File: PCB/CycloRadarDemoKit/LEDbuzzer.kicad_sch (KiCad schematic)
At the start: 27 parts, among them Q301 L8050QLT1G

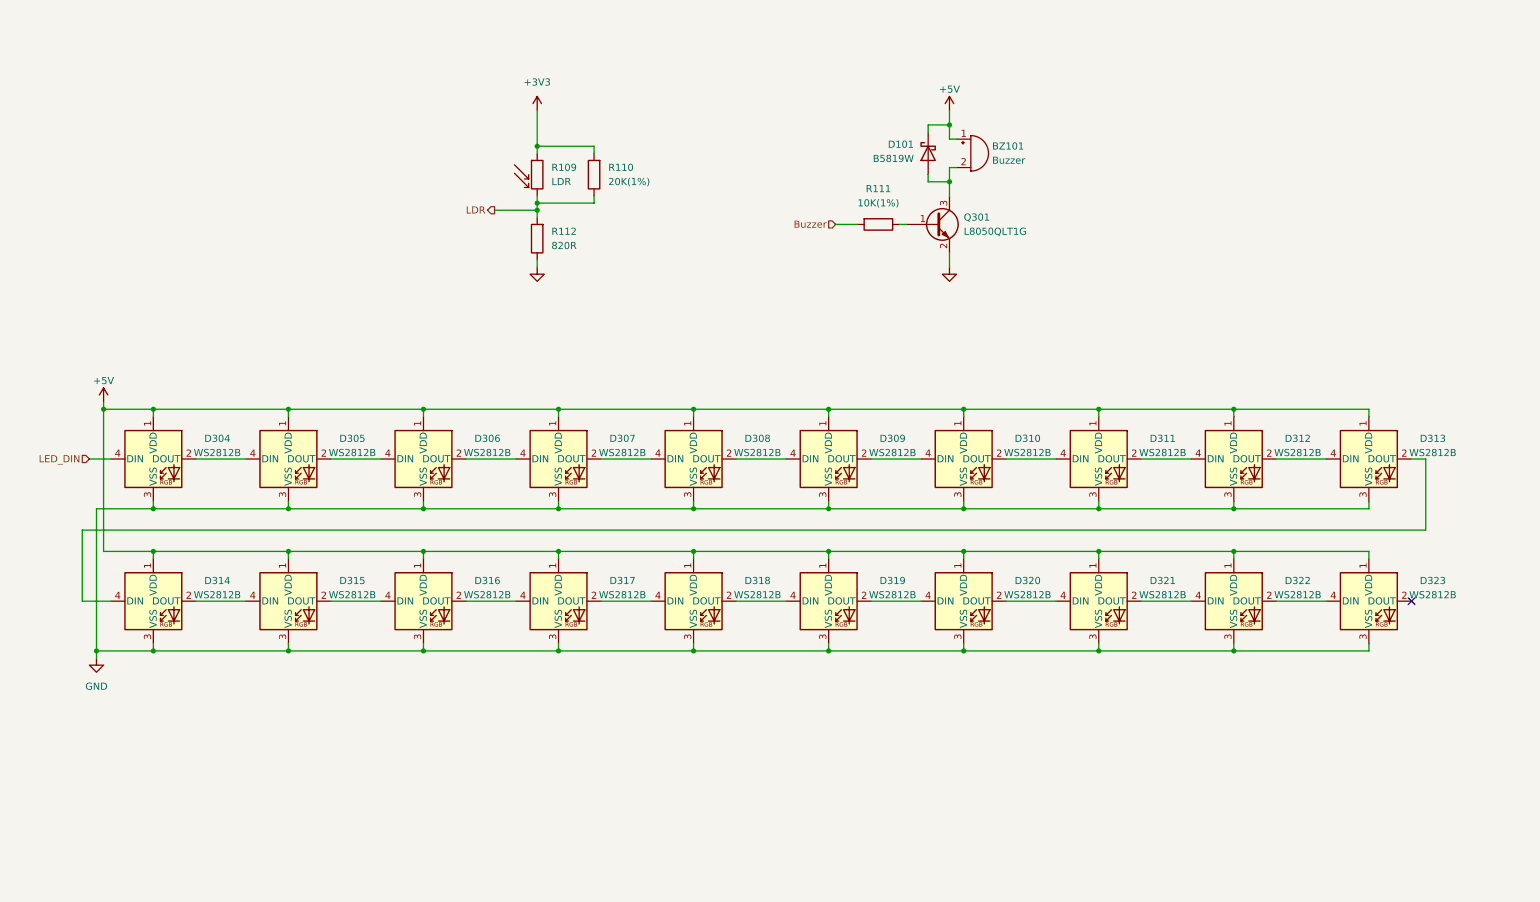
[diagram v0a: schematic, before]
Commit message: Schematic edited, split sheets
improved PM diagram
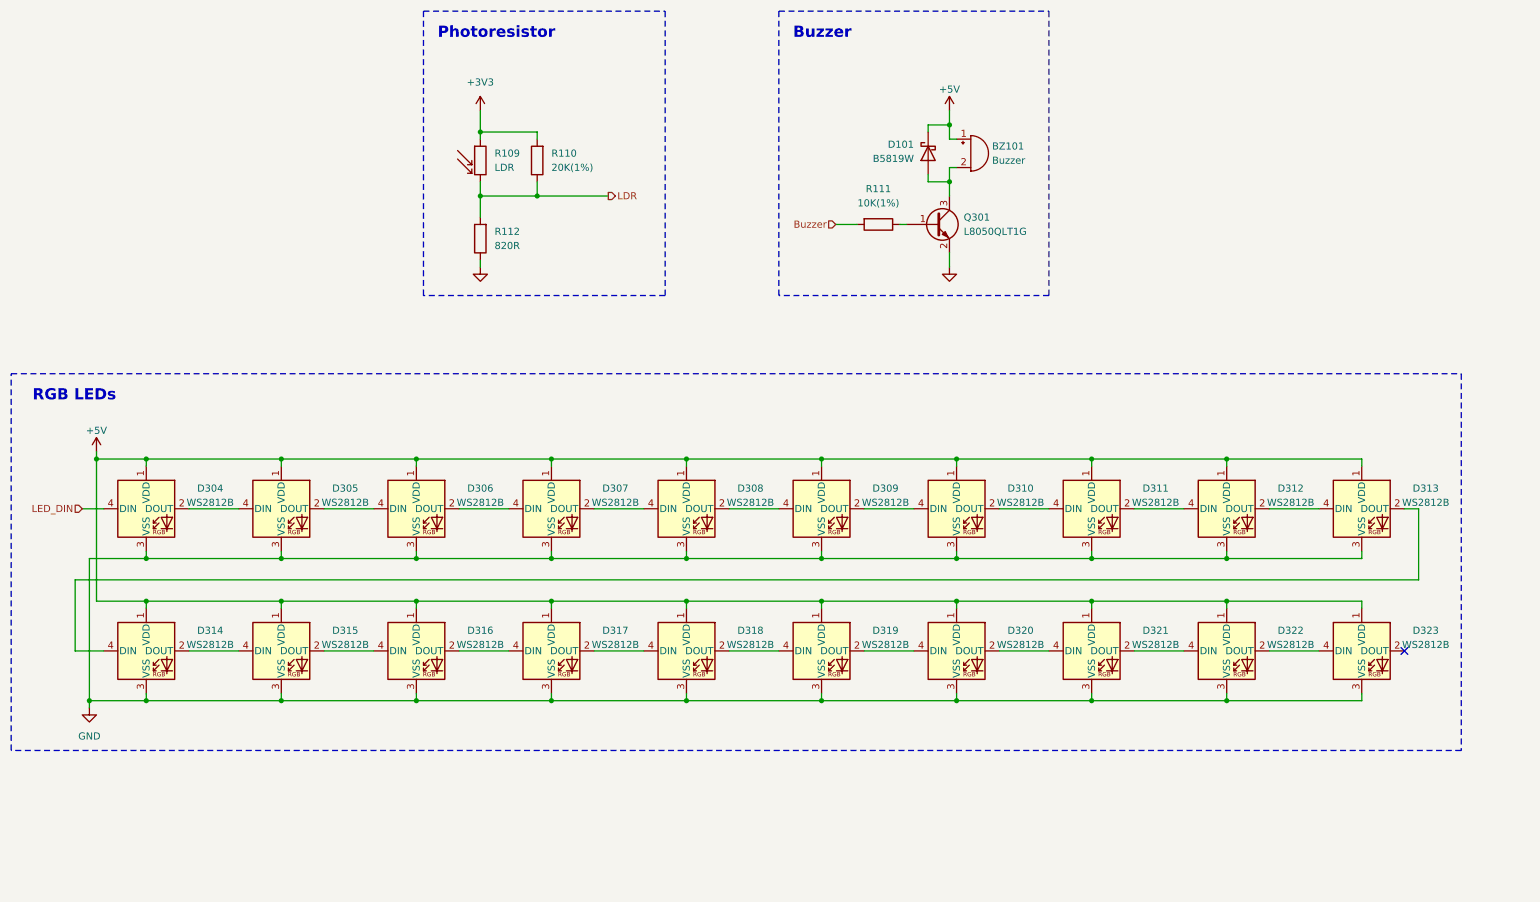
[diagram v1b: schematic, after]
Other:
- note added: "Buzzer"
- note added: "Photoresistor"
- note added: "RGB LEDs"
- moved on the sheet: D304, D305, D306, D307, D308, D309, D310, D311, D312, D313, D314, D315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

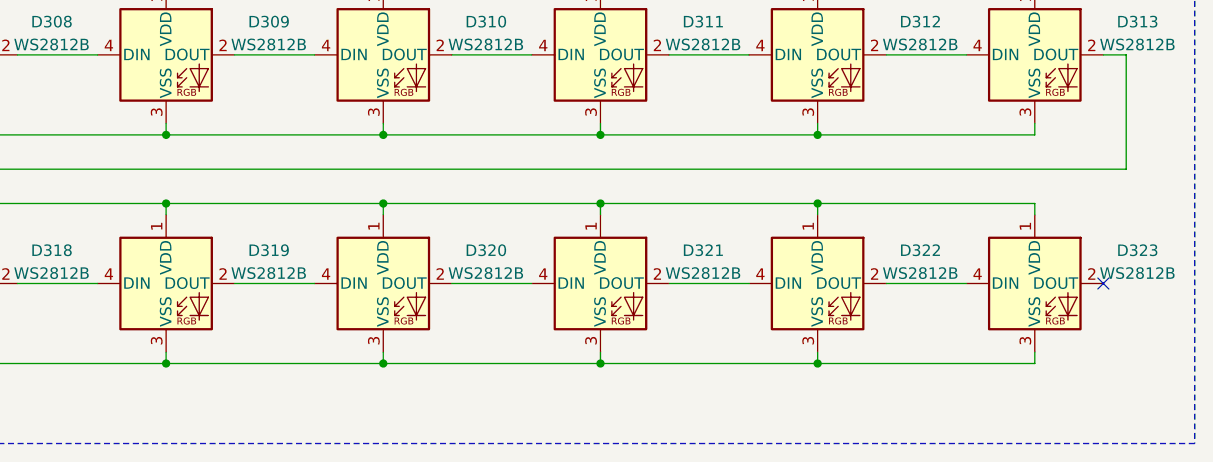
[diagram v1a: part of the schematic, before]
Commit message: layout mockup done
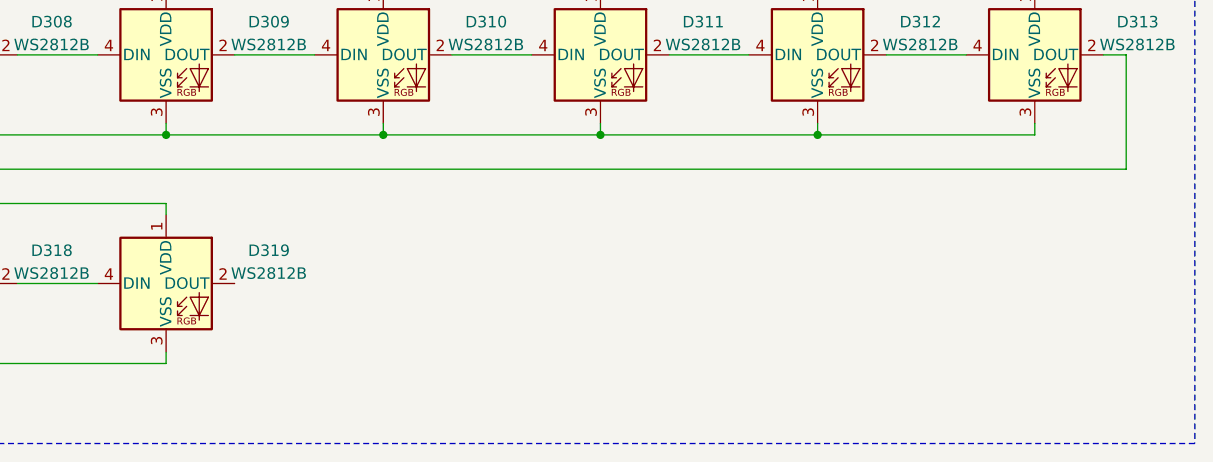
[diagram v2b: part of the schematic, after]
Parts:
- removed D320, D321, D322, D323: WS2812B, LED_SMD:LED_SK6812MINI_PLCC4_3.5x3.5mm_P1.75mm, symbol LED:WS2812B
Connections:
- no-connect marks 1 -> 0

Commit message: PCB, 3Dmodel
mockup PCB version done, schcematic exported to latex, 3D model generated and exported to latex
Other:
- title: Safety Ride Radar Sensor -> Radar Safety Sensor
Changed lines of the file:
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@@
   (paper "A4")
   (title_block
-    (title "Safety Ride Radar Sensor")
-    (date "2023-12-19")
-    (rev "Rev.: WIP")
+    (title "Radar Safety Sensor")
+    (date "2023-12-20")
+    (rev "Rev.: 1")
     (company "ALPS Electric Czech, s.r.o.")
     (comment 1 "Designed by Martin Tavoda")

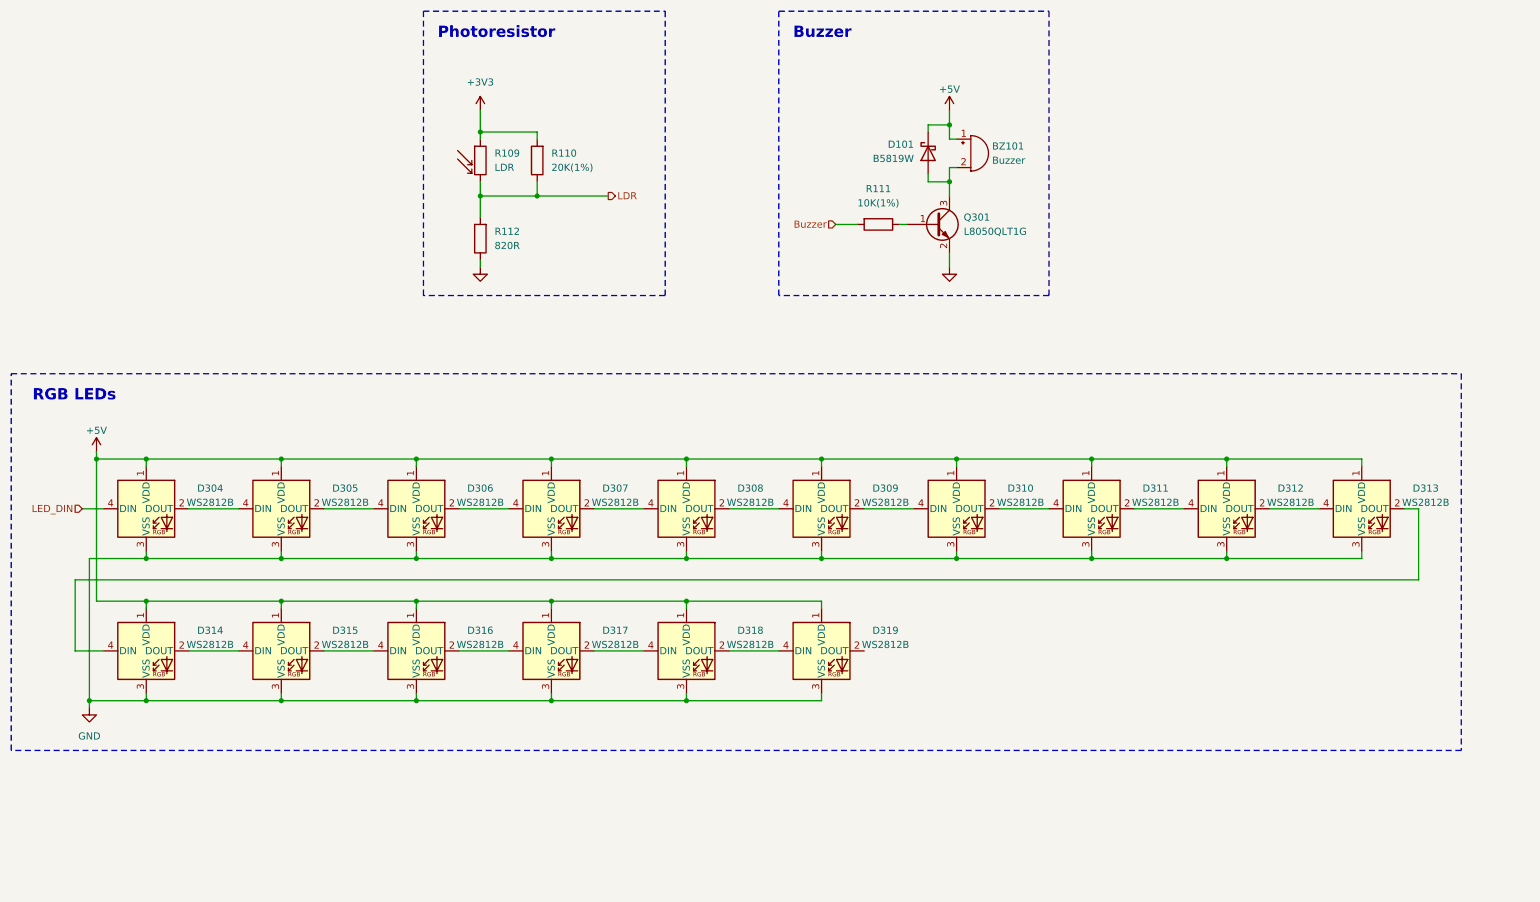
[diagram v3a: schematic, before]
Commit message: sortingAbbr, cosmetics schematic, export schematic to thesis
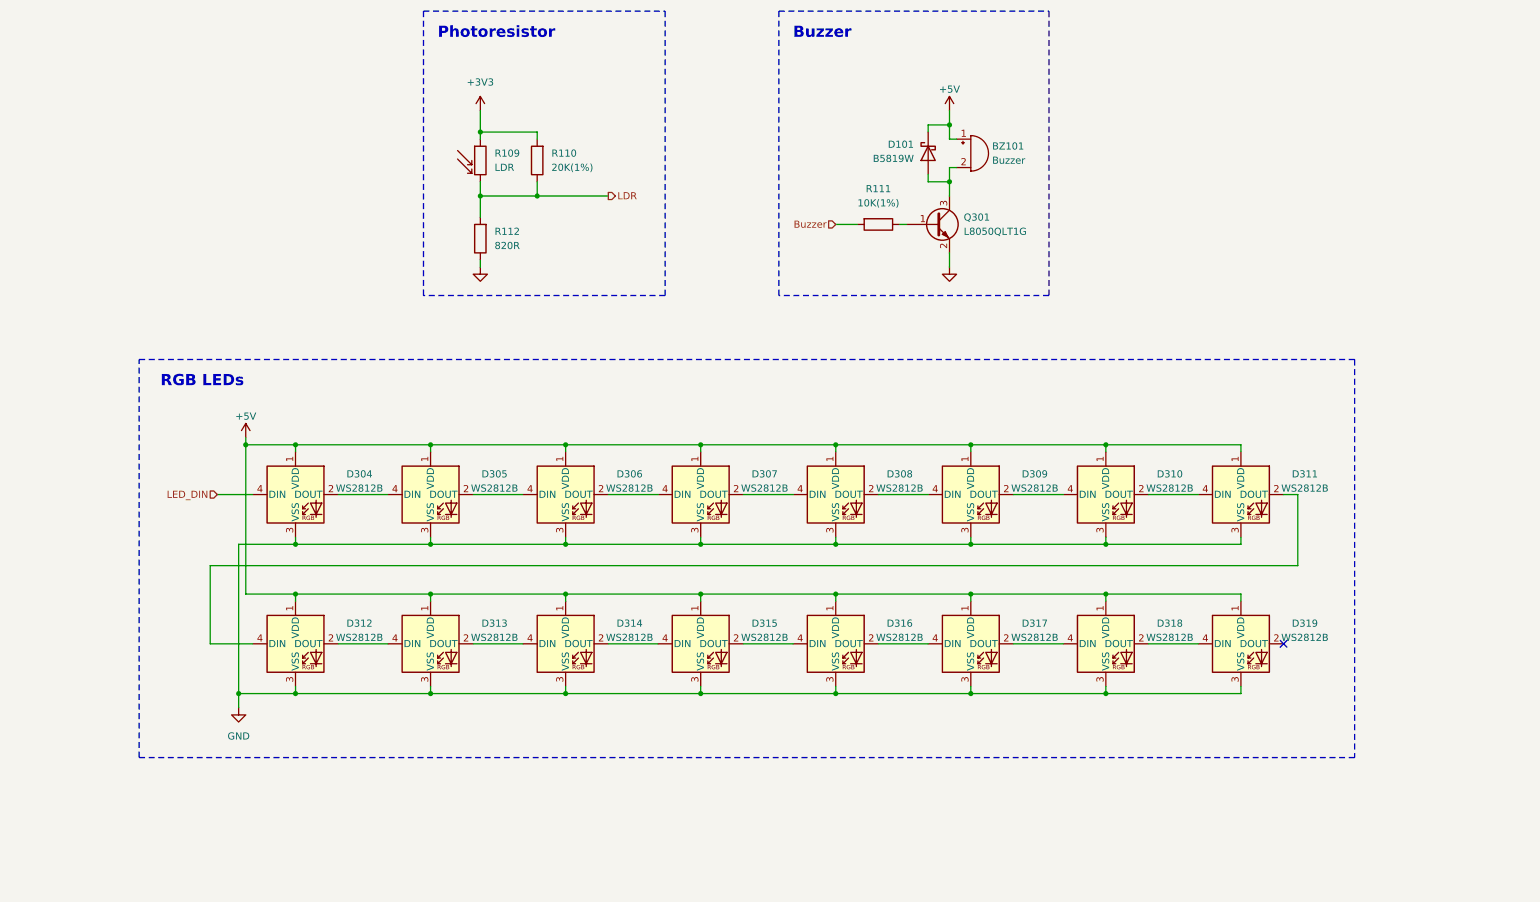
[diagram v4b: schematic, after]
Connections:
- no-connect marks 0 -> 1
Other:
- moved on the sheet: D304, D305, D306, D307, D308, D309, D310, D311, D312, D313, D314, D315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

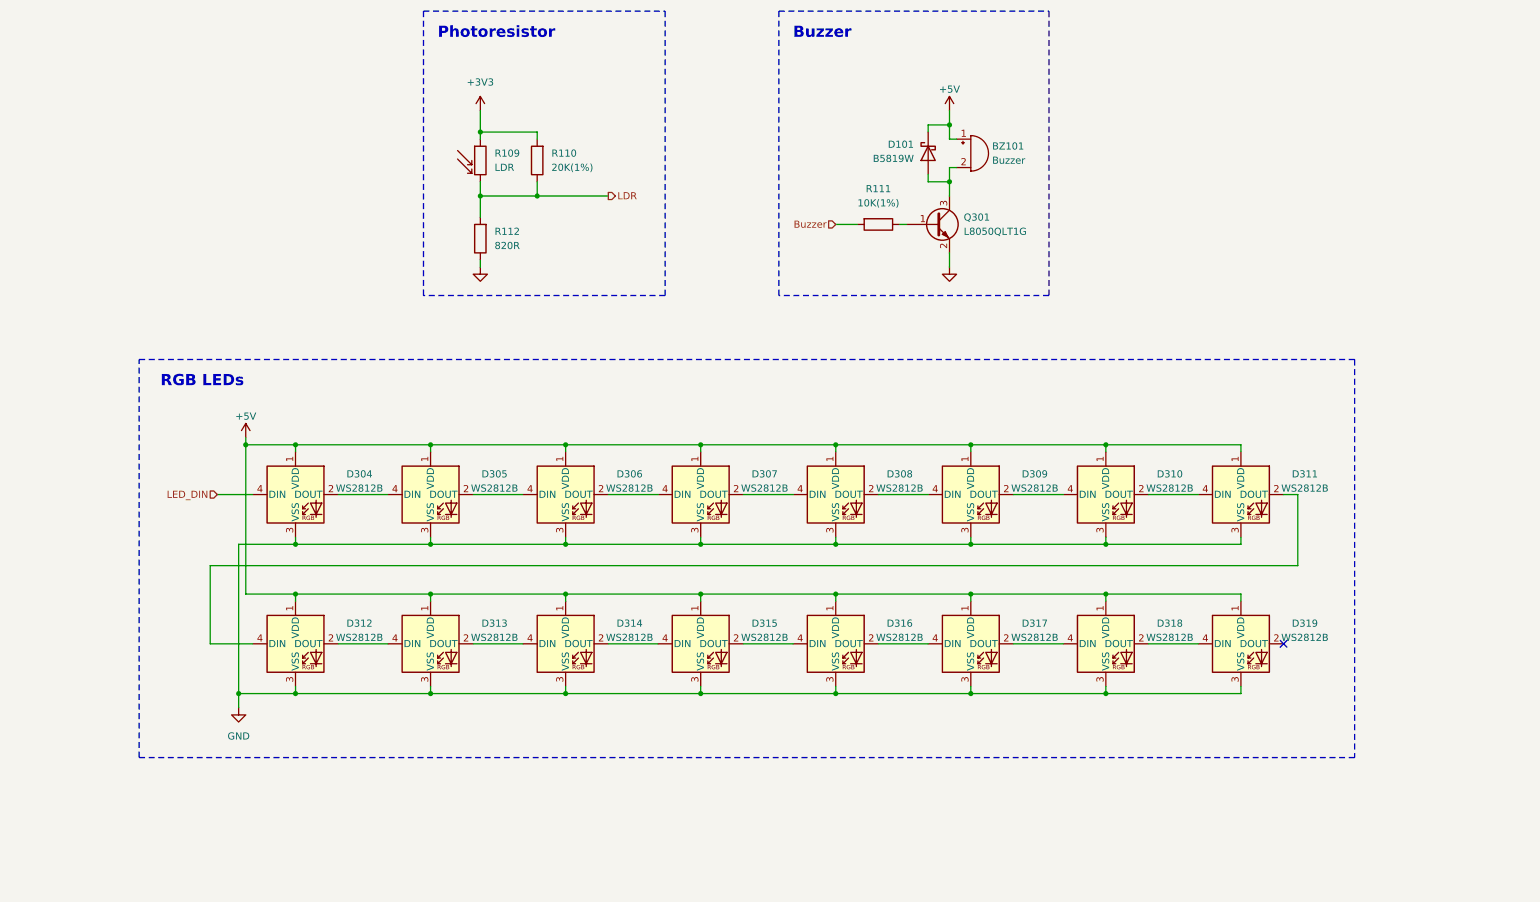
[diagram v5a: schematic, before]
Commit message: LEDs reodered, connectors moved
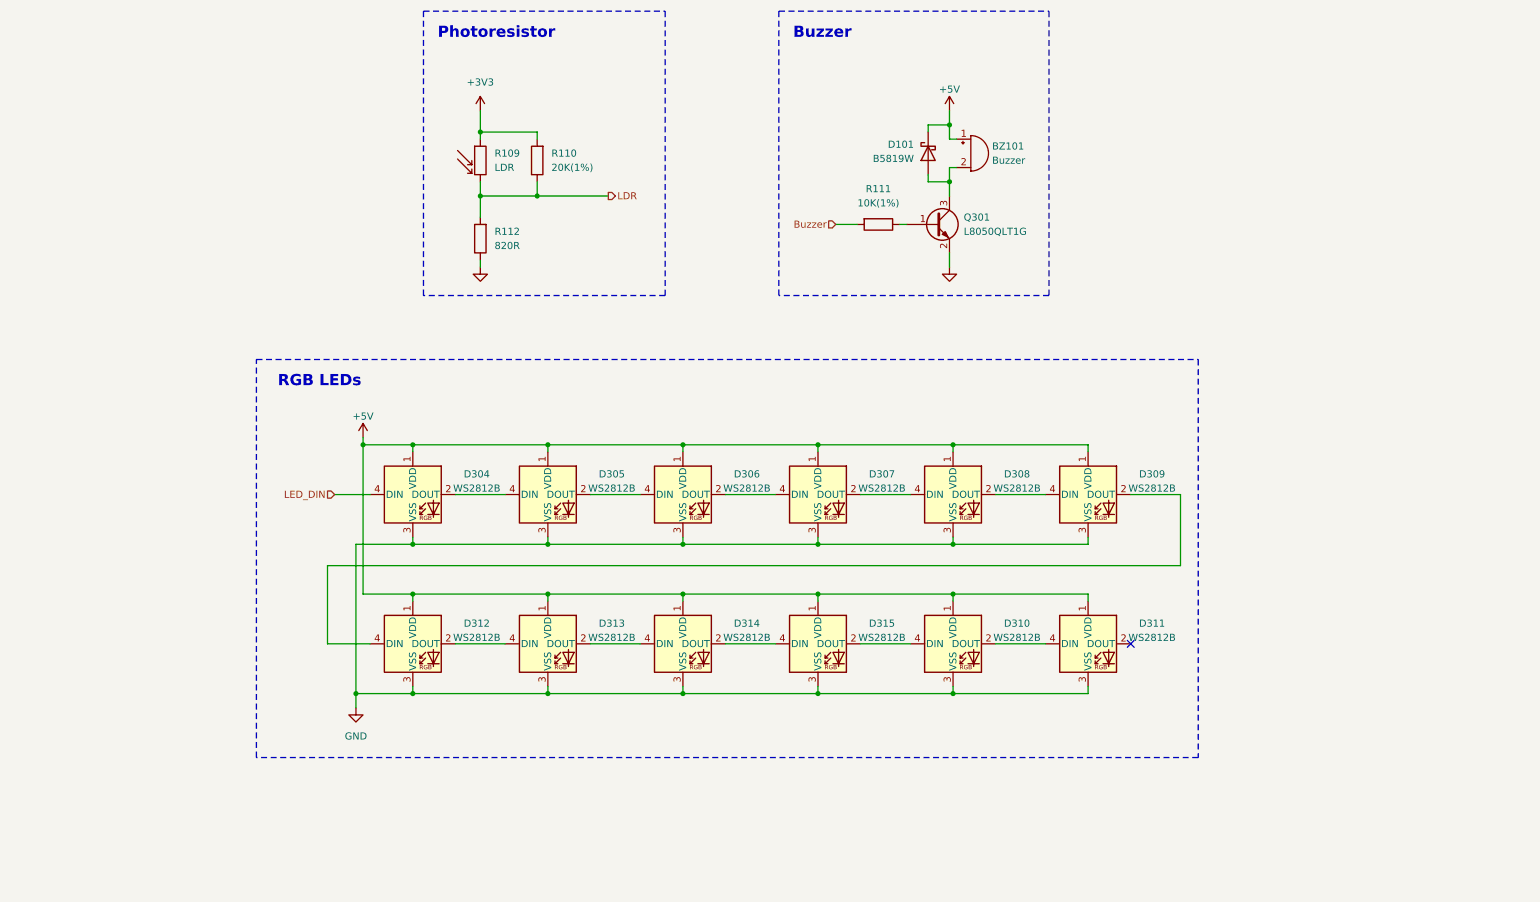
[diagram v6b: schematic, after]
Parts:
- removed D316, D317, D318, D319: WS2812B, LED_SMD:LED_SK6812MINI_PLCC4_3.5x3.5mm_P1.75mm, symbol LED:WS2812B
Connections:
- net at D315.2 (DOUT): now also D310.4 (DIN)
- net at D309.2 (DOUT): now also D312.4 (DIN); no longer D310.4 (DIN)
- net at D311.2 (DOUT): no longer D312.4 (DIN)
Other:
- moved on the sheet: D304, D305, D306, D307, D308, D309, D310, D311, D312, D313, D314, D315
